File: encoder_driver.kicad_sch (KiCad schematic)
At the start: 20 parts, among them J1 Conn_01x06_Male, J2 Conn_01x06_Male, J3 Conn_01x06, J4 Conn_01x02_Male, Q1 Si2319CDS, U1 TLE5012B, U2 ISO7321C, U3 ISO7320C, U4 B0505T-1W

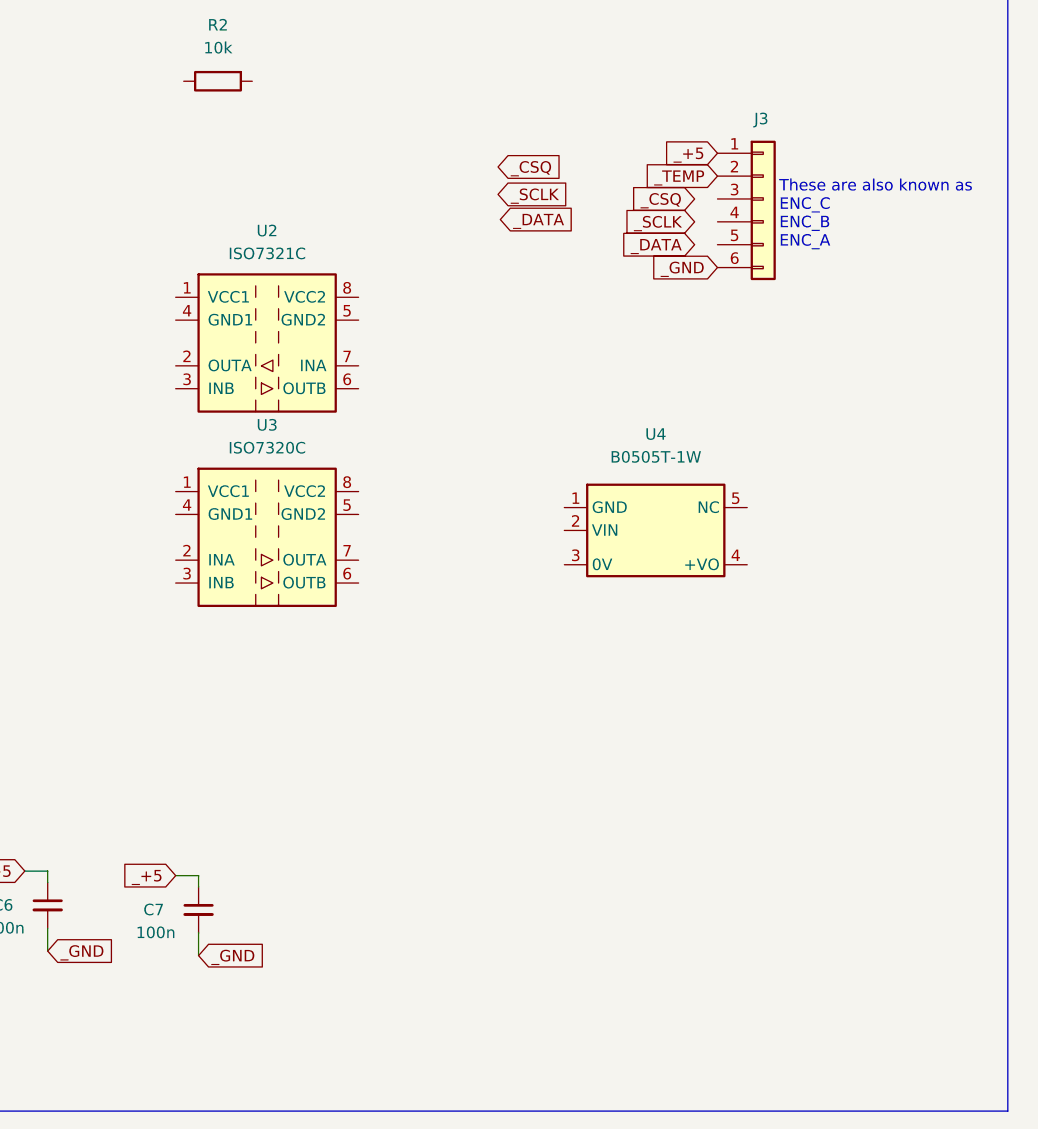
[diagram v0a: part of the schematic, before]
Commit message: TLE5012 encoder initialization
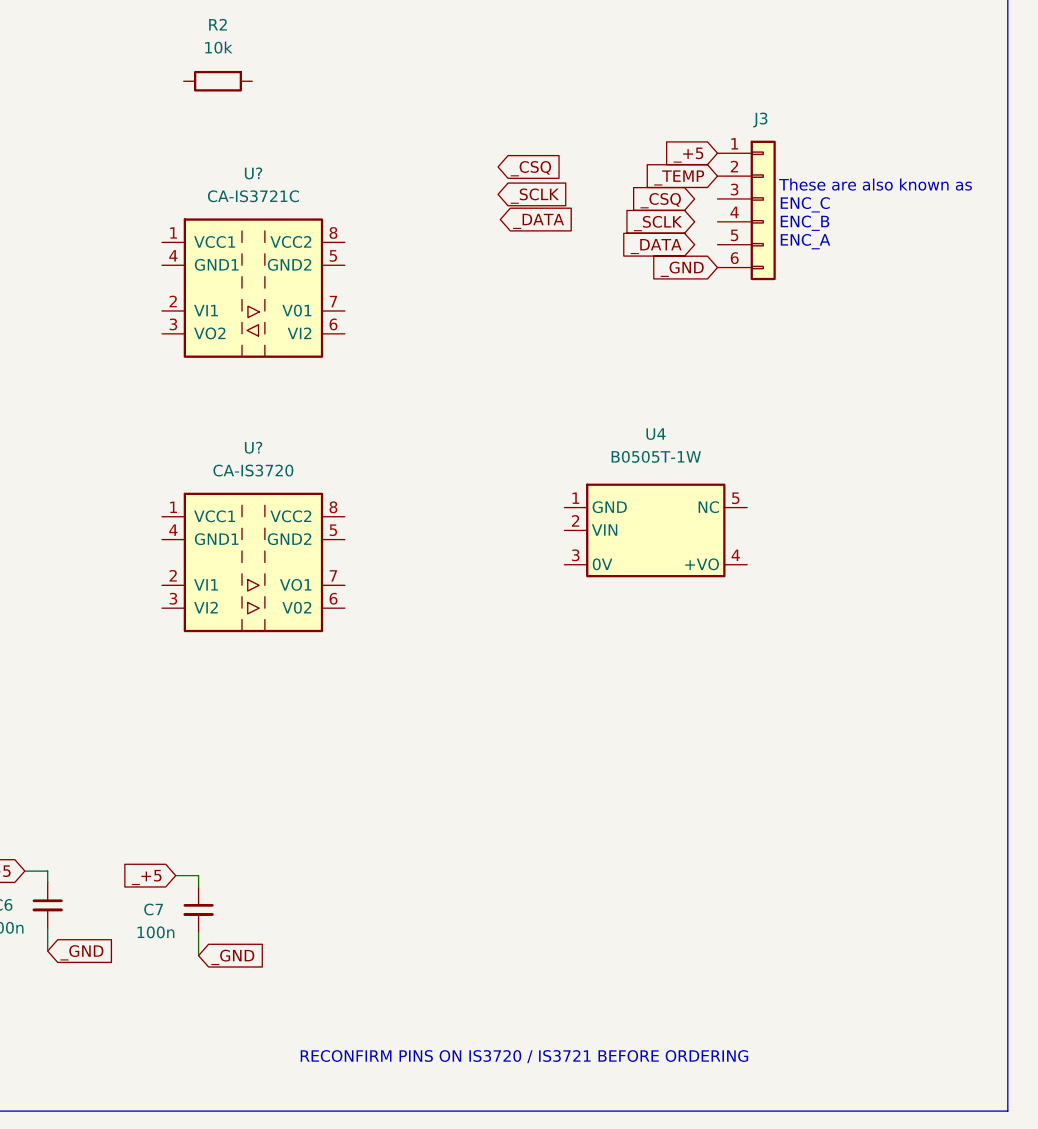
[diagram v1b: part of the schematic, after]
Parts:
- removed U2: ISO7321C, Package_SO:SOIC-8_3.9x4.9mm_P1.27mm, symbol Isolator:ISO7321C
- removed U3: ISO7320C, Package_SO:SOIC-8_3.9x4.9mm_P1.27mm, symbol Isolator:ISO7320C
- added U?: CA-IS3721C, Package_SO:SOIC-8_3.9x4.9mm_P1.27mm, symbol Isolator:CA-IS3721C
- added U?: CA-IS3720, Package_SO:SOIC-8_3.9x4.9mm_P1.27mm, symbol Isolator:CA-IS3720
- U4: LCSC (none) -> C30338
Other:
- note added: "RECONFIRM PINS ON IS3720 / IS3721 BEFORE ORDERING"

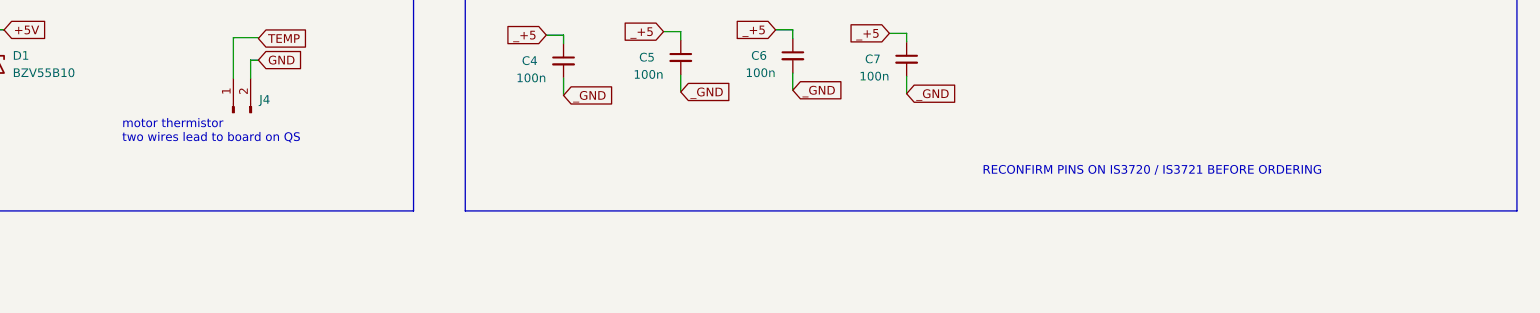
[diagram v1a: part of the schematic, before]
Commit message: TLE5012 encoder initialization
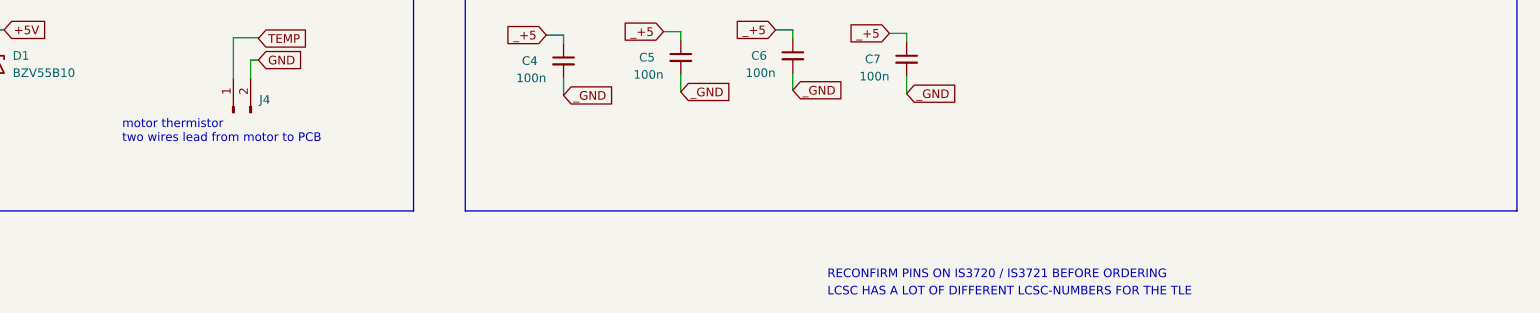
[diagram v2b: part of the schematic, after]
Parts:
- Q1: LCSC (none) -> C5122036
- U1: LCSC (none) -> C123083
- U?: LCSC (none) -> C428884
- U?: LCSC (none) -> C428882
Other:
- note added: "LCSC HAS A LOT OF DIFFERENT LCSC-NUMBERS FOR THE TLE"
- note added: "motor thermistor two wires lead from motor to PCB"
- note removed: "motor thermistor two wires lead to board on QS"
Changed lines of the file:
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@@
     (effects (font (size 7.62 7.62)) (justify left bottom))
   )
-  (text "motor thermistor\ntwo wires lead to board on QS" (at 76.454 150.114 0)
+  (text "motor thermistor\ntwo wires lead from motor to PCB" (at 76.454 150.114 0)
     (effects (font (size 1.27 1.27)) (justify left bottom))
   )
   (text "reverse polarity protection" (at 30.099 128.524 0)
+    (effects (font (size 1.27 1.27)) (justify left bottom))
+  )
+  (text "LCSC HAS A LOT OF DIFFERENT LCSC-NUMBERS FOR THE TLE"
+    (at 180.34 172.72 0)
     (effects (font (size 1.27 1.27)) (justify left bottom))
   )
@@
     (effects (font (size 1.27 1.27)) (justify left bottom))
   )
-  (text "RECONFIRM PINS ON IS3720 / IS3721 BEFORE ORDERING" (at 203.2 154.94 0)
+  (text "RECONFIRM PINS ON IS3720 / IS3721 BEFORE ORDERING" (at 180.34 170.18 0)
     (effects (font (size 1.27 1.27)) (justify left bottom))
   )
@@
     )
     (property "Datasheet" " https://www.infineon.com/dgdl/Infineon-TLE5012B_Exxxx-DataSheet-v02_01-EN.pdf" (id 3) (at 107.569 117.221 0)
+      (effects (font (size 1.27 1.27)) hide)
+    )
+    (property "LCSC" "C123083" (id 4) (at 52.959 76.581 0)
       (effects (font (size 1.27 1.27)) hide)
     )
@@
       (effects (font (size 1.27 1.27) italic) hide)
     )
-    (property "Datasheet" "http://www.ti.com/general/docs/lit/getliterature.tsp?genericPartNumber=iso7321c&fileType=pdf" (id 3) (at 198.5772 79.8068 0)
+    (property "Datasheet" "" (id 3) (at 198.5772 79.8068 0)
+      (effects (font (size 1.27 1.27)) hide)
+    )
+    (property "LCSC" "C428884" (id 4) (at 198.12 68.58 0)
       (effects (font (size 1.27 1.27)) hide)
     )
@@
       (effects (font (size 1.27 1.27)) (justify left) hide)
     )
+    (property "LCSC" "C5122036" (id 4) (at 51.435 135.89 0)
+      (effects (font (size 1.27 1.27)) hide)
+    )
     (pin "1")
     (pin "2")
@@
       (effects (font (size 1.27 1.27) italic) hide)
     )
-    (property "Datasheet" "http://www.ti.com/general/docs/lit/getliterature.tsp?genericPartNumber=iso7320c&fileType=pdf" (id 3) (at 198.12 109.22 0)
-      (effects (font (size 1.27 1.27)) hide)
-    )
+    (property "Datasheet" "" (id 3) (at 198.12 109.22 0)
+      (effects (font (size 1.27 1.27)) hide)
+    )
+    (property "LCSC" "C428882" (id 4) (at 198.12 99.06 0)
+      (effects (font (size 1.27 1.27)) hide)
+    )

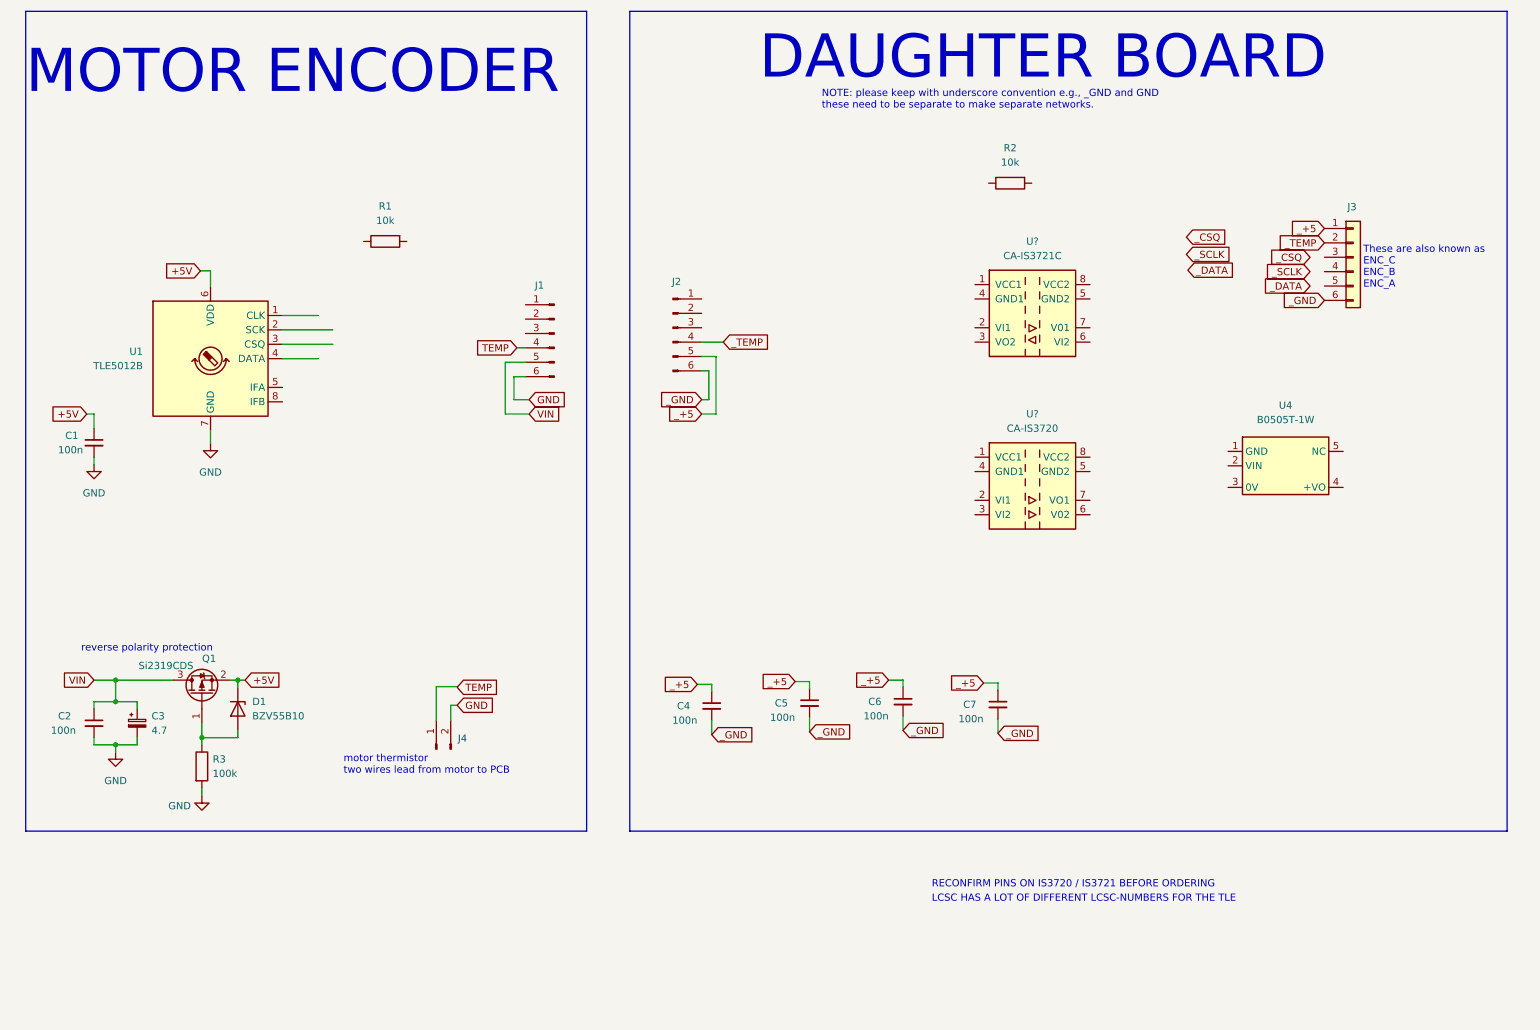
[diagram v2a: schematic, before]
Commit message: added isolators
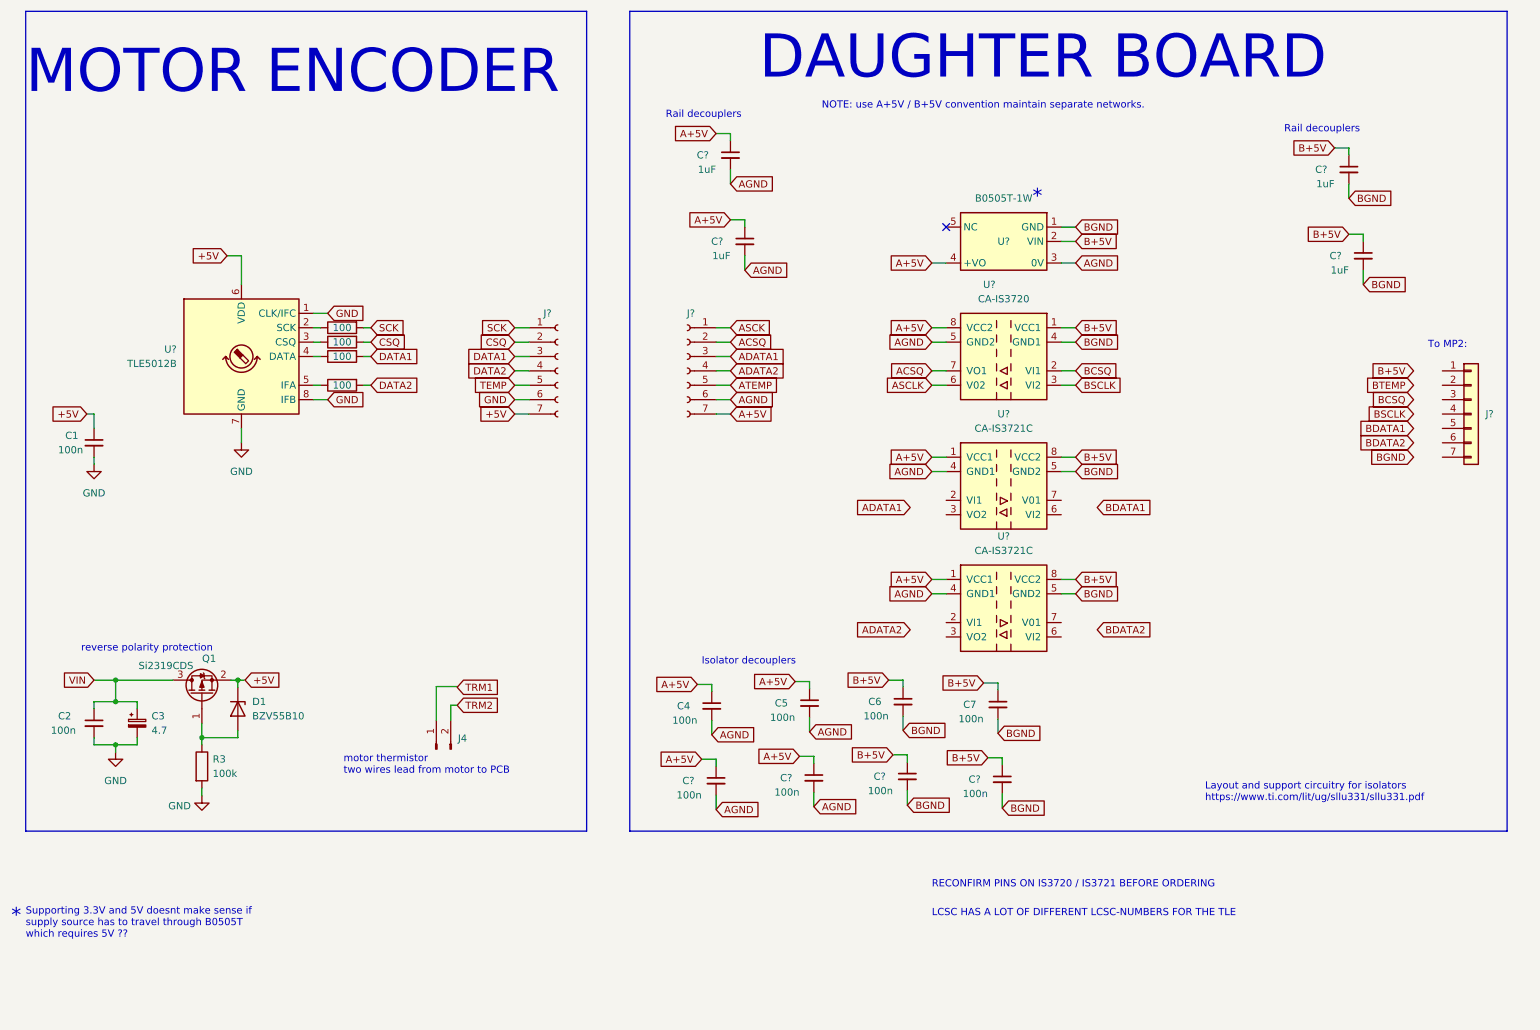
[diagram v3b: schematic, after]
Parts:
- removed J1, J2: Conn_01x06_Male, Connector_PinHeader_2.54mm:PinHeader_1x06_P2.54mm_Vertical, symbol Connector:Conn_01x06_Male
- removed J3: Conn_01x06, Connector_JST:my_JST_1x06_P2.00mm_Vertical, symbol Connector_Generic:Conn_01x06
- removed R2: 10k, Resistor_SMD:R_0603_1608Metric, symbol Device:R
- removed U1: TLE5012B, Package_SO:SOIC-8_3.9x4.9mm_P1.27mm, symbol Sensor_Magnetic:TLE5012B
- removed U4: B0505T-1W, EASY_EDA:PWRM-SMD_B0505XT-1WR2, symbol Converter_DCDC:B0505T-1W
- removed U?: CA-IS3721C, Package_SO:SOIC-8_3.9x4.9mm_P1.27mm, symbol Isolator:CA-IS3721C
- removed U?: CA-IS3720, Package_SO:SOIC-8_3.9x4.9mm_P1.27mm, symbol Isolator:CA-IS3720
- added C? (x4): 1uF, Capacitor_SMD:C_0603_1608Metric, symbol Device:C_Small
- added C? (x4): 100n, Capacitor_SMD:C_0603_1608Metric, symbol Device:C_Small
- added J? (x2): Conn_01x07_Female, symbol Connector:Conn_01x07_Female
- added J?: Conn_01x07, symbol Connector_Generic:Conn_01x07
- added R? (x3): 100, Resistor_SMD:R_0603_1608Metric, symbol Device:R
- added U? (x2): CA-IS3721C, Package_SO:SOIC-8_3.9x4.9mm_P1.27mm, symbol Isolator:CA-IS3721C
- added U?: CA-IS3720, Package_SO:SOIC-8_3.9x4.9mm_P1.27mm, symbol Isolator:CA-IS3720
- added U?: B0505T-1W, EASY_EDA:PWRM-SMD_B0505XT-1WR2, symbol Converter_DCDC:B0505T-1W
- added U?: TLE5012B, Package_SO:Infineon_PG-DSO-8-27_3.9x4.9mm_EP2.65x3mm, symbol Sensor_Magnetic:TLE5012B
- R1: value 10k -> 100
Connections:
- net +5V: now also J?.7 (Pin_7), U?.6 (VDD)
- net GND: now also J?.6 (Pin_6), U?.1 (CLK/IFC), U?.7 (GND), U?.8 (IFB); no longer J4.2 (Pin_2)
- net TEMP: now also J?.5 (Pin_5)
- net at R1.1: now also U?.2 (SCK)
- net SCK: now reaches R1.2
- net SCK: now also J?.1 (Pin_1)
- net _+5 renamed A+5V
- net A+5V: now also C?.1, C?.1, C?.1, C?.1, J?.7 (Pin_7), U?.1 (VCC1), U?.1 (VCC1), U?.4 (+VO), U?.8 (VCC2); no longer C6.1, C7.1
- net _GND renamed AGND
- net AGND: now also C?.2, C?.2, C?.2, C?.2, J?.6 (Pin_6), U?.3 (0V), U?.4 (GND1), U?.4 (GND1), U?.5 (GND2); no longer C6.2, C7.2
- new net: R?.1, U?.3 (CSQ)
- new net: R?.1, U?.4 (DATA)
- new net: R?.1, U?.5 (IFA)
- new net ACSQ: J?.2 (Pin_2), U?.7 (VO1)
- new net ADATA1: J?.3 (Pin_3)
- new net ADATA2: J?.4 (Pin_4)
- new net ASCK: J?.1 (Pin_1)
- new net ASCLK: U?.6 (V02)
- new net ATEMP: J?.5 (Pin_5)
- new net B+5V: C6.1, C7.1, C?.1, C?.1, C?.1, C?.1, U?.1 (VCC1), U?.2 (VIN), U?.8 (VCC2), U?.8 (VCC2)
- new net BCSQ: U?.2 (VI1)
- new net BGND: C6.2, C7.2, C?.2, C?.2, C?.2, C?.2, U?.1 (GND), U?.4 (GND1), U?.5 (GND2), U?.5 (GND2)
- new net BSCLK: U?.3 (VI2)
- new net CSQ: J?.2 (Pin_2), R?.2
- new net DATA1: J?.3 (Pin_3), R?.2
- new net DATA2: J?.4 (Pin_4), R?.2
- new net TRM2: J4.2 (Pin_2)
- no-connect marks 0 -> 1
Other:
- note added: "*"
- note added: "Isolator decouplers"
- note added: "Layout and support circuitry for isolators https://www.ti.com/lit/ug/sllu331/sllu331.pdf"
- note added: "NOTE: use A+5V / B+5V convention maintain separate networks."
- note added: "Rail decouplers"
- note added: "Supporting 3.3V and 5V doesnt make sense if supply source has to travel through B0505T which requires 5V ??"
- note added: "To MP2:"
- note removed: "NOTE: please keep with underscore convention e.g., _GND and GND these need to be separate to make separate networks."
- note removed: "These are also known as ENC_C ENC_B ENC_A"
